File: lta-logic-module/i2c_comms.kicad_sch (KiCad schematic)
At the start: 12 parts

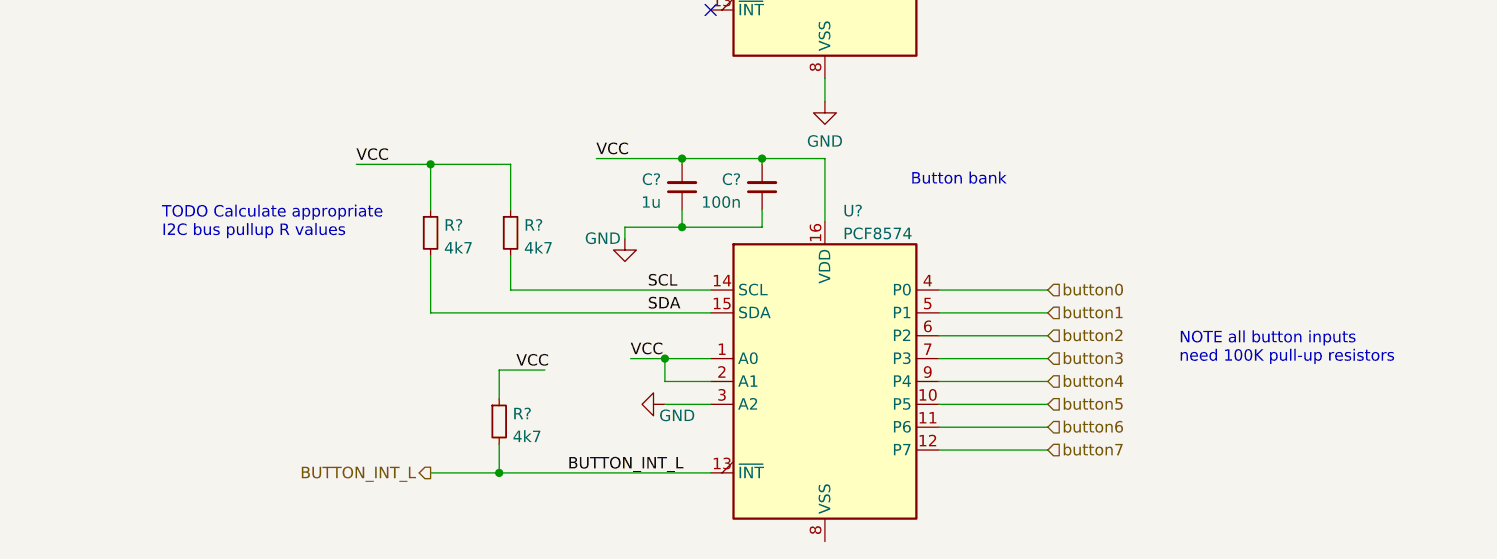
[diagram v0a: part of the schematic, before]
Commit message: Full sketch of logic module schematic.
- Add button inputs
- Add LED signal driver / PWM combination
- Add 5V regulator based on LM2592
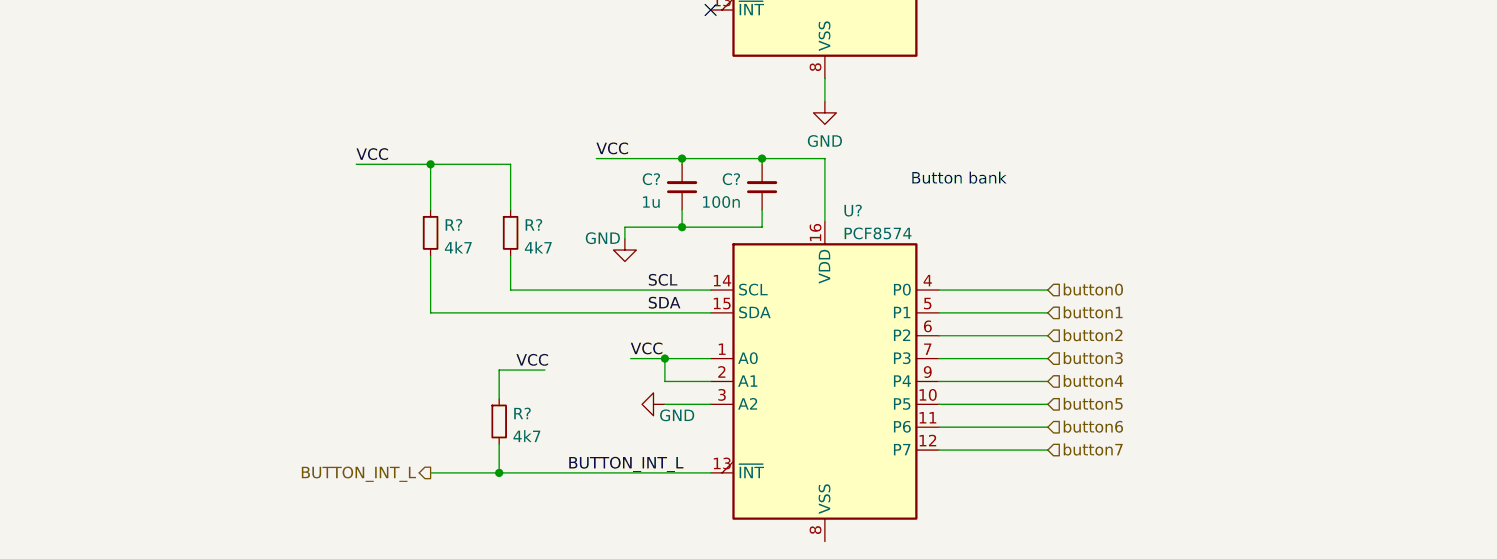
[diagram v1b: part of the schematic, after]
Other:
- note removed: "NOTE all button inputs need 100K pull-up resistors"
- note removed: "TODO Calculate appropriate I2C bus pullup R values"
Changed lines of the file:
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@@
     (stroke (width 0) (type default) (color 0 0 0 0))
-  )
-  (text "TODO Calculate appropriate\nI2C bus pullup R values"
-    (at 36.83 136.525 0)
-    (effects (font (size 1.27 1.27)) (justify left bottom))
   )
   (text "MOSFET bank 1\n\n" (at 120.015 83.82 0)
@@
     (effects (font (size 1.27 1.27)) (justify left bottom))
   )
-  (text "NOTE all button inputs\nneed 100K pull-up resistors"
-    (at 149.86 150.495 0)
-    (effects (font (size 1.27 1.27)) (justify left bottom))
-  )

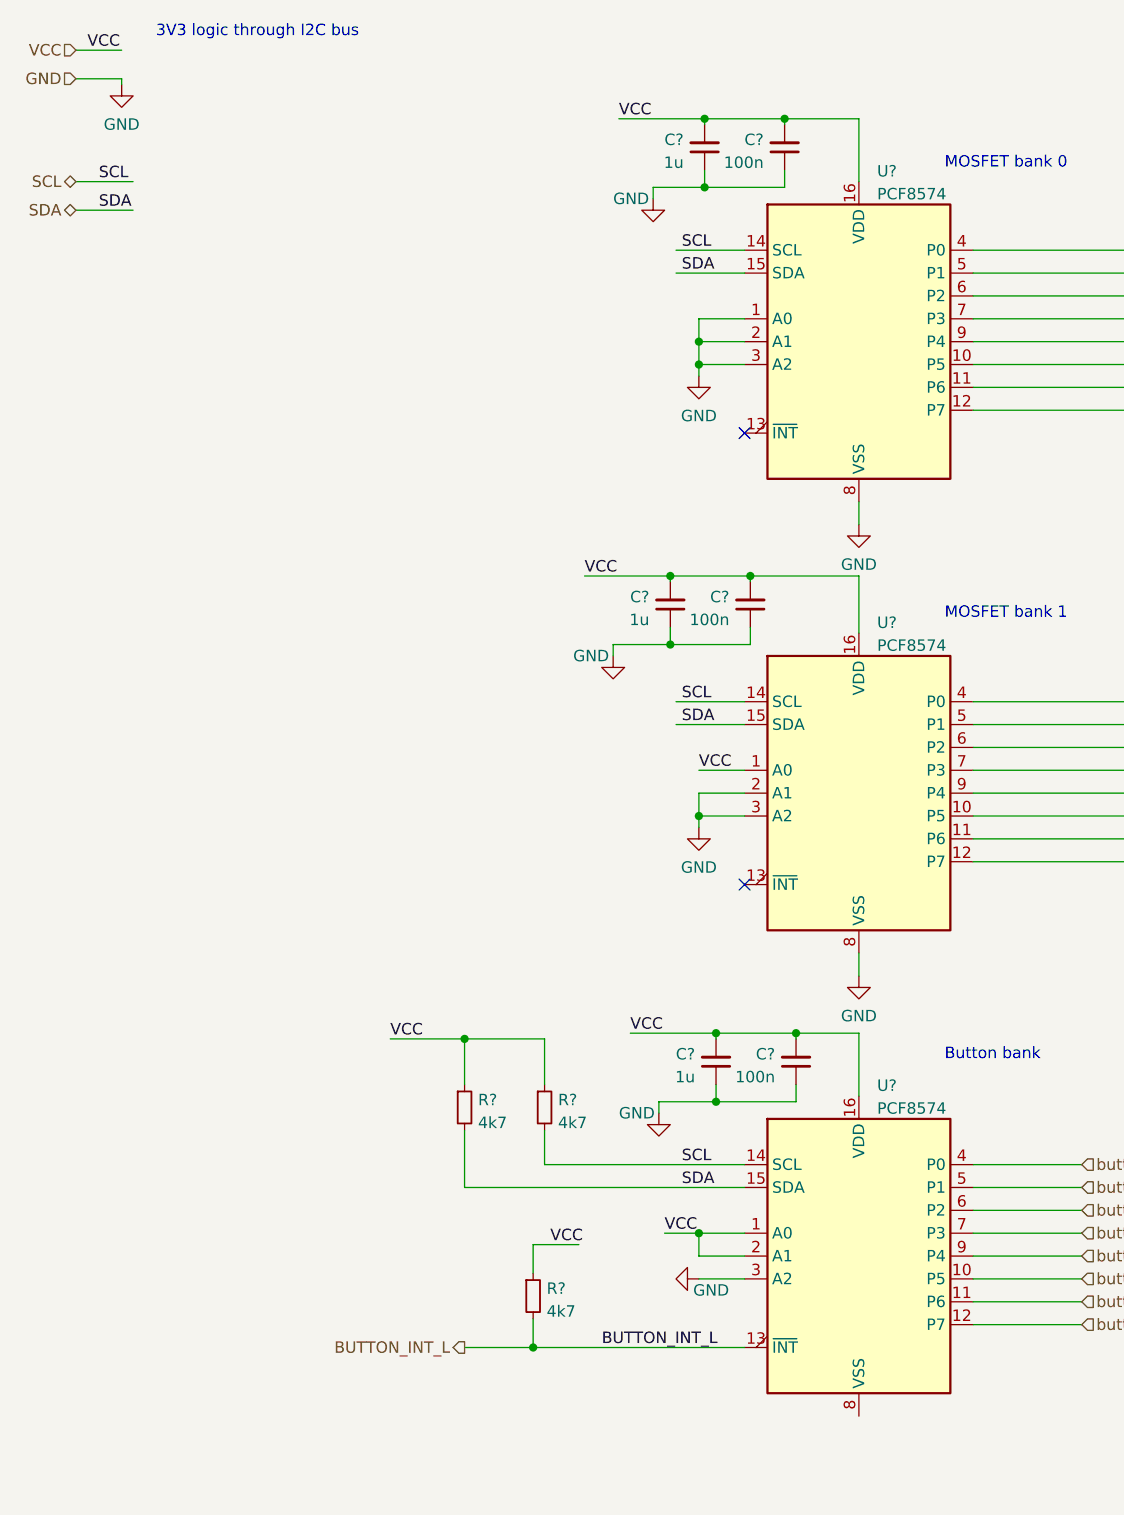
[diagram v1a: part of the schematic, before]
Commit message: Fix ERC violations.
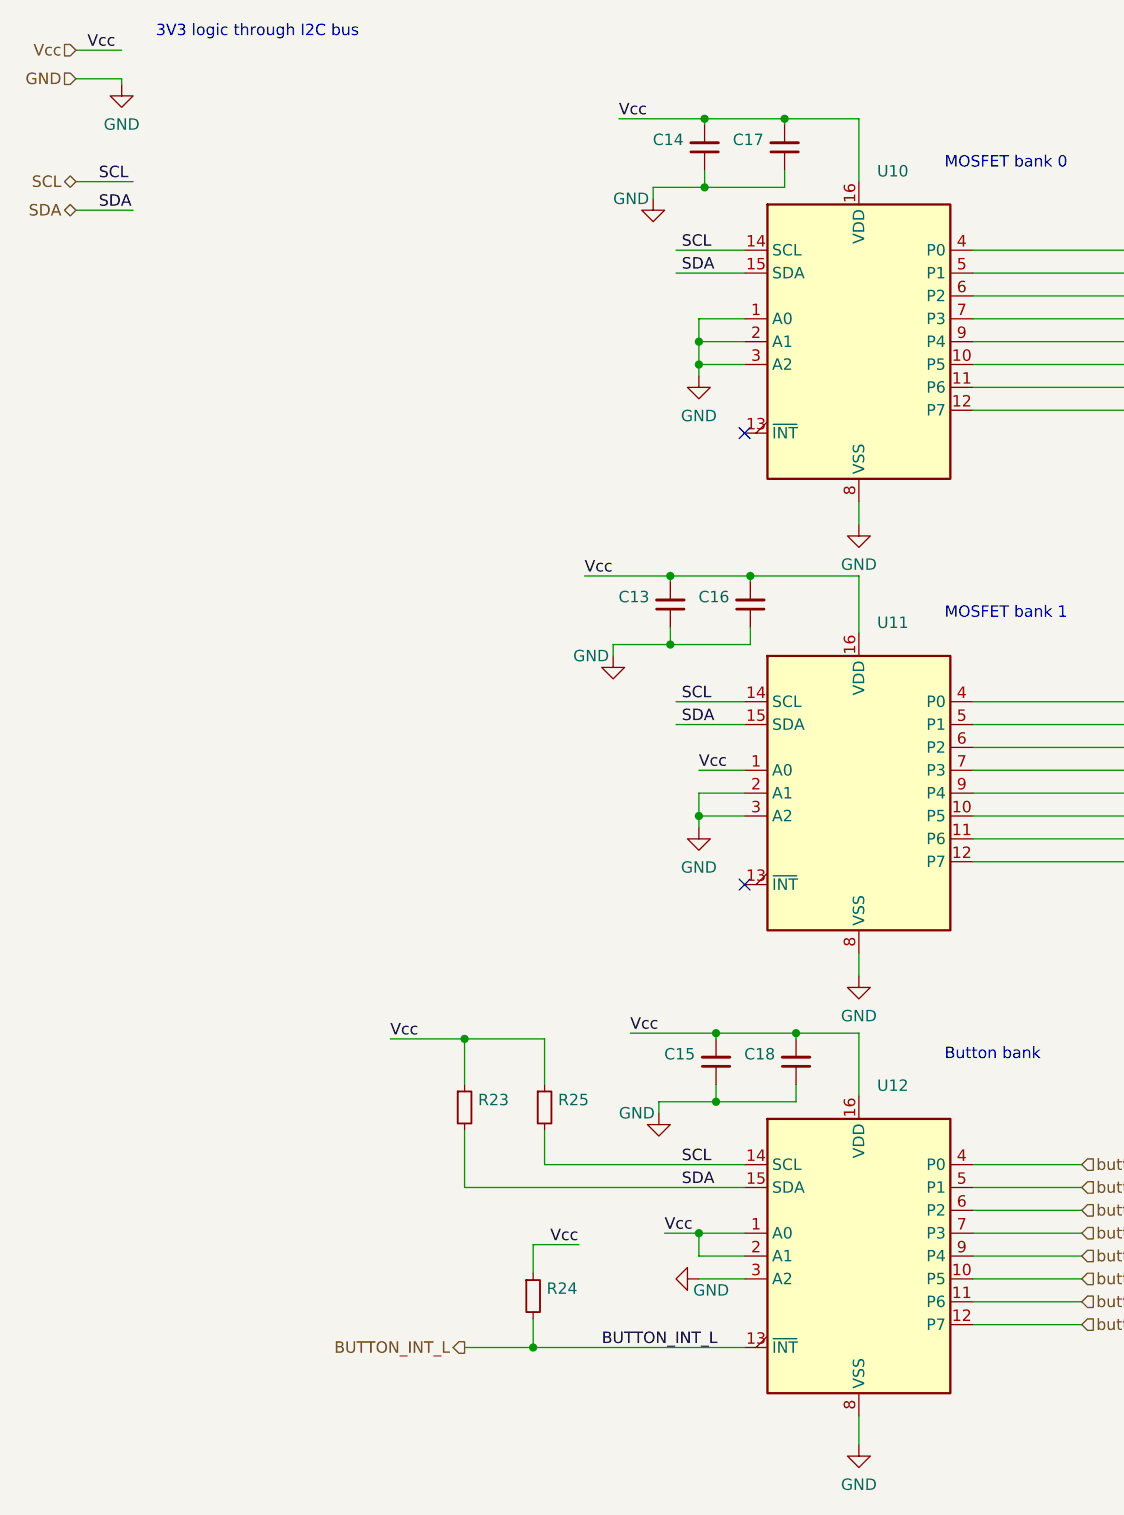
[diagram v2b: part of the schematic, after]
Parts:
- C13, C14, C15: renamed from C?; value 1u -> (none)
- C16, C17, C18: renamed from C?; value 100n -> (none)
- R23, R24, R25: renamed from R?; value 4k7 -> (none)
- U10, U11, U12: renamed from U?; value PCF8574 -> (none)
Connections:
- net GND: now also U12.8 (VSS)
- net VCC renamed Vcc

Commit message: Add TODOs, update some footprints.
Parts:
- C13, C14, C15: value (none) -> 1u; footprint (none) -> Capacitor_SMD:C_0603_1608Metric; Comment (none) -> 1u 5% 16V 0603 X7R ceramic; 20mOhm < ESR < 10 Ohm; MANUFACTURER (none) -> KYOCERA; MPN (none) -> 0603YC105JAT2A
- C16, C17, C18: value (none) -> 100n; footprint (none) -> Capacitor_SMD:C_0603_1608Metric; Comment (none) -> 100nF 5% 6.3V 0603 X7R ceramic; 20mOhm < ESR < 10 Ohm; MANUFACTURER (none) -> KYOCERA; MPN (none) -> 06036C104JAT2A
- R23, R24, R25: value (none) -> 4K7; footprint (none) -> Resistor_SMD:R_0603_1608Metric; Comment (none) -> 4K7 0603 resistor; +/-1%; 1/10W; MANUFACTURER (none) -> YAEGO; MPN (none) -> RC0603FR-074K7L
- U10, U11, U12: value (none) -> PCF8574; footprint (none) -> Aaron_TI_Parts:TI_SOIC_DW0016A; MANUFACTURER (none) -> Texas Instruments; MPN (none) -> PCF8574DW

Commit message: Initial PCB setup
* Configure Elecrow DRC checks for lta-logic-module.
* Switch SN74LVC244A from 'N' PDIP to 'DWR' SOIC footprint.
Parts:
- renumbered C17 to C10, C18 to C11, C13 to C6, C14 to C7, C15 to C8, C16 to C9, R23 to R3, R24 to R4, R25 to R5, U10 to U3, U11 to U4, U12 to U5
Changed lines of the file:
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@@
   (symbol (lib_id "power:GND") (at 92.71 104.775 0) (unit 1)
     (in_bom yes) (on_board yes) (fields_autoplaced)
-    (property "Reference" "#PWR046" (id 0) (at 92.71 111.125 0)
+    (property "Reference" "#PWR027" (id 0) (at 92.71 111.125 0)
       (effects (font (size 1.27 1.27)) hide)
     )
@@
   (symbol (lib_id "power:GND") (at 110.49 121.285 0) (unit 1)
     (in_bom yes) (on_board yes) (fields_autoplaced)
-    (property "Reference" "#PWR049" (id 0) (at 110.49 127.635 0)
+    (property "Reference" "#PWR030" (id 0) (at 110.49 127.635 0)
       (effects (font (size 1.27 1.27)) hide)
     )
@@
   (symbol (lib_id "power:GND") (at 110.49 173.355 0) (unit 1)
     (in_bom yes) (on_board yes) (fields_autoplaced)
-    (property "Reference" "#PWR050" (id 0) (at 110.49 179.705 0)
+    (property "Reference" "#PWR031" (id 0) (at 110.49 179.705 0)
       (effects (font (size 1.27 1.27)) hide)
     )
@@
   (symbol (lib_id "Device:R_Small") (at 75.565 135.89 0) (unit 1)
     (in_bom yes) (on_board yes) (fields_autoplaced)
-    (property "Reference" "R25" (id 0) (at 77.0636 135.0553 0)
+    (property "Reference" "R5" (id 0) (at 77.0636 135.0553 0)
       (effects (font (size 1.27 1.27)) (justify left))
     )
@@
   (symbol (lib_id "power:GND") (at 92.71 154.94 270) (unit 1)
     (in_bom yes) (on_board yes)
-    (property "Reference" "#PWR047" (id 0) (at 86.36 154.94 0)
+    (property "Reference" "#PWR028" (id 0) (at 86.36 154.94 0)
       (effects (font (size 1.27 1.27)) hide)
     )
@@
   (symbol (lib_id "Device:C_Small") (at 103.505 130.81 0) (mirror x) (unit 1)
     (in_bom yes) (on_board yes) (fields_autoplaced)
-    (property "Reference" "C18" (id 0) (at 101.1809 129.9689 0)
+    (property "Reference" "C11" (id 0) (at 101.1809 129.9689 0)
       (effects (font (size 1.27 1.27)) (justify right))
     )
@@
   (symbol (lib_id "Device:R_Small") (at 74.295 156.845 0) (unit 1)
     (in_bom yes) (on_board yes) (fields_autoplaced)
-    (property "Reference" "R24" (id 0) (at 75.7936 156.0103 0)
+    (property "Reference" "R4" (id 0) (at 75.7936 156.0103 0)
       (effects (font (size 1.27 1.27)) (justify left))
     )
@@
   (symbol (lib_id "power:GND") (at 110.49 71.12 0) (unit 1)
     (in_bom yes) (on_board yes) (fields_autoplaced)
-    (property "Reference" "#PWR048" (id 0) (at 110.49 77.47 0)
+    (property "Reference" "#PWR029" (id 0) (at 110.49 77.47 0)
       (effects (font (size 1.27 1.27)) hide)
     )
@@
   (symbol (lib_id "Device:C_Small") (at 89.535 80.01 0) (mirror x) (unit 1)
     (in_bom yes) (on_board yes) (fields_autoplaced)
-    (property "Reference" "C13" (id 0) (at 87.2109 79.1689 0)
+    (property "Reference" "C6" (id 0) (at 87.2109 79.1689 0)
       (effects (font (size 1.27 1.27)) (justify right))
     )
@@
   (symbol (lib_id "power:GND") (at 88.265 136.525 0) (unit 1)
     (in_bom yes) (on_board yes)
-    (property "Reference" "#PWR044" (id 0) (at 88.265 142.875 0)
+    (property "Reference" "#PWR025" (id 0) (at 88.265 142.875 0)
       (effects (font (size 1.27 1.27)) hide)
     )
@@
   (symbol (lib_id "Device:C_Small") (at 93.345 29.21 0) (mirror x) (unit 1)
     (in_bom yes) (on_board yes) (fields_autoplaced)
-    (property "Reference" "C14" (id 0) (at 91.0209 28.3689 0)
+    (property "Reference" "C7" (id 0) (at 91.0209 28.3689 0)
       (effects (font (size 1.27 1.27)) (justify right))
     )
@@
   (symbol (lib_id "Device:C_Small") (at 98.425 80.01 0) (mirror x) (unit 1)
     (in_bom yes) (on_board yes) (fields_autoplaced)
-    (property "Reference" "C16" (id 0) (at 96.1009 79.1689 0)
+    (property "Reference" "C9" (id 0) (at 96.1009 79.1689 0)
       (effects (font (size 1.27 1.27)) (justify right))
     )
@@
   (symbol (lib_id "Device:C_Small") (at 102.235 29.21 0) (mirror x) (unit 1)
     (in_bom yes) (on_board yes) (fields_autoplaced)
-    (property "Reference" "C17" (id 0) (at 99.9109 28.3689 0)
+    (property "Reference" "C10" (id 0) (at 99.9109 28.3689 0)
       (effects (font (size 1.27 1.27)) (justify right))
     )
@@
   (symbol (lib_id "power:GND") (at 87.63 34.925 0) (unit 1)
     (in_bom yes) (on_board yes)
-    (property "Reference" "#PWR043" (id 0) (at 87.63 41.275 0)
+    (property "Reference" "#PWR024" (id 0) (at 87.63 41.275 0)
       (effects (font (size 1.27 1.27)) hide)
     )
@@
   (symbol (lib_id "Interface_Expansion:PCF8574") (at 110.49 100.965 0) (unit 1)
     (in_bom yes) (on_board yes) (fields_autoplaced)
-    (property "Reference" "U11" (id 0) (at 112.5094 82.0252 0)
+    (property "Reference" "U4" (id 0) (at 112.5094 82.0252 0)
       (effects (font (size 1.27 1.27)) (justify left))
     )
@@
   (symbol (lib_id "power:GND") (at 28.575 22.225 0) (unit 1)
     (in_bom yes) (on_board yes) (fields_autoplaced)
-    (property "Reference" "#PWR041" (id 0) (at 28.575 28.575 0)
+    (property "Reference" "#PWR022" (id 0) (at 28.575 28.575 0)
       (effects (font (size 1.27 1.27)) hide)
     )
@@
   (symbol (lib_id "Device:R_Small") (at 66.675 135.89 0) (unit 1)
     (in_bom yes) (on_board yes) (fields_autoplaced)
-    (property "Reference" "R23" (id 0) (at 68.1736 135.0553 0)
+    (property "Reference" "R3" (id 0) (at 68.1736 135.0553 0)
       (effects (font (size 1.27 1.27)) (justify left))
     )
@@
   (symbol (lib_id "power:GND") (at 92.71 54.61 0) (unit 1)
     (in_bom yes) (on_board yes) (fields_autoplaced)
-    (property "Reference" "#PWR045" (id 0) (at 92.71 60.96 0)
+    (property "Reference" "#PWR026" (id 0) (at 92.71 60.96 0)
       (effects (font (size 1.27 1.27)) hide)
     )
@@
   (symbol (lib_id "Interface_Expansion:PCF8574") (at 110.49 50.8 0) (unit 1)
     (in_bom yes) (on_board yes) (fields_autoplaced)
-    (property "Reference" "U10" (id 0) (at 112.5094 31.8602 0)
+    (property "Reference" "U3" (id 0) (at 112.5094 31.8602 0)
       (effects (font (size 1.27 1.27)) (justify left))
     )
@@
   (symbol (lib_id "power:GND") (at 83.185 85.725 0) (unit 1)
     (in_bom yes) (on_board yes)
-    (property "Reference" "#PWR042" (id 0) (at 83.185 92.075 0)
+    (property "Reference" "#PWR023" (id 0) (at 83.185 92.075 0)
       (effects (font (size 1.27 1.27)) hide)
     )
@@
   (symbol (lib_id "Device:C_Small") (at 94.615 130.81 0) (mirror x) (unit 1)
     (in_bom yes) (on_board yes) (fields_autoplaced)
-    (property "Reference" "C15" (id 0) (at 92.2909 129.9689 0)
+    (property "Reference" "C8" (id 0) (at 92.2909 129.9689 0)
       (effects (font (size 1.27 1.27)) (justify right))
     )
@@
   (symbol (lib_id "Interface_Expansion:PCF8574") (at 110.49 152.4 0) (unit 1)
     (in_bom yes) (on_board yes) (fields_autoplaced)
-    (property "Reference" "U12" (id 0) (at 112.5094 133.4602 0)
-      (effects (font (size 1.27 1.27)) (justify left))
-    )
+    (property "Reference" "U5" (id 0) (at 112.5094 133.4602 0)
+      (effects (font (size 1.27 1.27)) (justify left))
+    )
